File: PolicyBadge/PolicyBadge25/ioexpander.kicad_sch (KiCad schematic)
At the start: 25 parts, among them Q1 2N7002, U10 YX-SMD5020, U9 TCA9555PWR

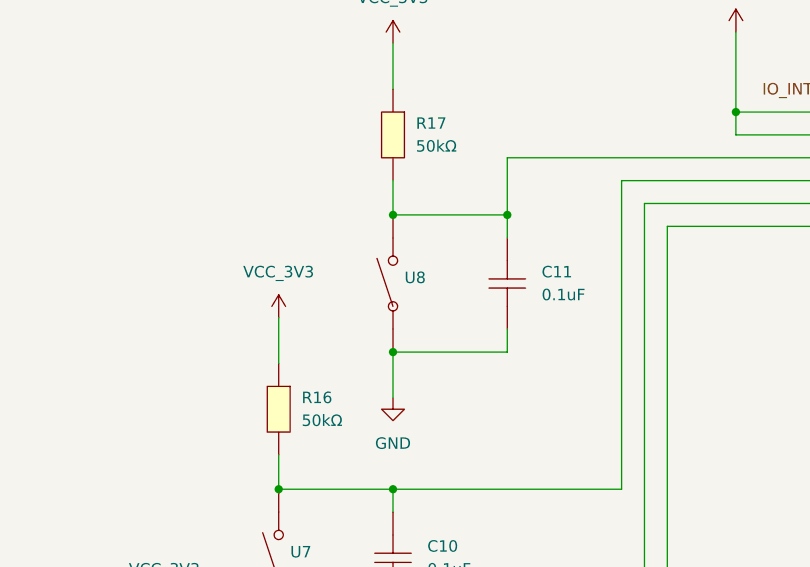
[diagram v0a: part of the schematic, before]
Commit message: removed U5 switch from schematic
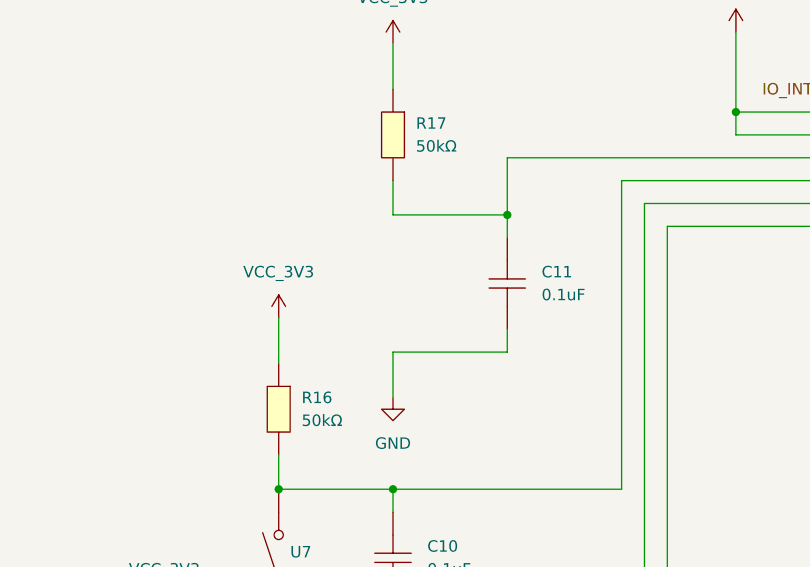
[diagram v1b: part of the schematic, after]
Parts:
- removed U8: ~, imported:SW-TH_HRO_K2-1109DF-EXXW-XX, symbol JLCPCB:K2-1109DF-E4SW-04
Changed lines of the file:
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@@
-	)
-	(junction
-		(at 96.52 64.77)
-		(diameter 0)
-		(color 0 0 0 0)
 	)
 	(junction
@@
 	(junction
 		(at 58.42 161.29)
-		(diameter 0)
-		(color 0 0 0 0)
-	)
-	(junction
-		(at 96.52 80.01)
 		(diameter 0)
 		(color 0 0 0 0)
@@
 					(unit 1)
 				)
-			)
-		)
-	)
-	(symbol
-		(lib_id "JLCPCB:K2-1109DF-E4SW-04")
-		(at 96.52 72.39 90)
-		(unit 1)
-		(exclude_from_sim no)
-		(in_bom yes)
-		(on_board yes)
-		(dnp no)
-		(fields_autoplaced yes)
-		(property "Reference" "U8"
-			(at 97.79 71.7549 90)
-			(effects
-				(font
-					(size 1.27 1.27)
-				)
-				(justify right)
-			)
-		)
-		(property "Value" "~"
-			(at 97.79 73.66 90)
-			(effects
-				(font
-					(size 1.27 1.27)
-				)
-				(justify right)
-			)
-		)
-		(property "Footprint" "imported:SW-TH_HRO_K2-1109DF-EXXW-XX"
-			(at 104.14 72.39 0)
-			(effects
-				(font
-					(size 1.27 1.27)
-				)
-				(hide yes)
-			)
-		)
-		(property "Datasheet" ""
-			(at 96.52 72.39 0)
-			(effects
-				(font
-					(size 1.27 1.27)
-				)
-				(hide yes)
-			)
-		)
-		(property "Description" ""
-			(at 96.52 72.39 0)
-			(effects
-				(font
-					(size 1.27 1.27)
-				)
-				(hide yes)
-			)
-		)
-		(property "LCSC Part" "C2909684"
-			(at 106.68 72.39 0)
-			(effects
-				(font
-					(size 1.27 1.27)
-				)
-				(hide yes)
-			)
-		)
-		(property "MPN" "K2-1109DF-E4SW-04"
-			(at 96.52 72.39 0)
-			(effects
-				(font
-					(size 1.27 1.27)
-				)
-				(hide yes)
-			)
-		)
-		(pin "2"
-		)
-		(pin "1"
-		)
-		(instances
-			(project "PolicyBadge25"
-				(path "/3911717a-8f19-42c2-8f04-ebfae4e12db6/0606a99a-a678-47a5-968e-d91d30829907"
-					(reference "U8")
-					(unit 1)
-				)
